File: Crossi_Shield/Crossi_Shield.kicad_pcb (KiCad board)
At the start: 4 copper layers, 86 parts, among them IC1 TPS54540DDAR, IC2 TCAN1048AVDMTRQ1, IC3 TCAN1048AVDMTRQ1, IC4 TCAN1048AVDMTRQ1, J1 Raspberry_Pi_2_3, J2 10090926-P444VLF, SW1 SW_DIP_x01

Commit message: Fast fertig gerouted
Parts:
- added H8: MountingHole, MountingHole:MountingHole_3.2mm_M3_DIN965_Pad, F.Cu at (141.5, 103.5)
- added H9: MountingHole, MountingHole:MountingHole_3.2mm_M3_DIN965_Pad, F.Cu at (141.5, 152.5)
- JP1, JP2, JP3, JP4, JP5: moved to B.Cu
- moved R6 69.6 mm to (144.6, 111.5), turned to 180 degrees
- moved D3 62.4 mm to (140.4, 111.5), turned to 0 degrees
- moved SW1 48.5 mm to (143.2, 115.5), turned to 180 degrees
- moved D5 34.4 mm to (83.0, 117.6), turned to 0 degrees
- moved R8 31.3 mm to (86.9, 117.6), turned to 180 degrees
- moved D6 30.1 mm to (83.0, 115.5), turned to 0 degrees
- moved R9 26.9 mm to (86.9, 115.5), turned to 180 degrees
- moved D7 26.1 mm to (83.0, 113.3), turned to 0 degrees
- moved R14 25.5 mm to (145.2, 139.2)
- moved R10 22.5 mm to (86.9, 113.3), turned to 180 degrees
- moved D8 22.1 mm to (83.0, 111.2), turned to 0 degrees
- moved R15 20.9 mm to (145.2, 141.2)
- moved IC2 19.1 mm to (136.7, 138.5)
- moved D4 18.5 mm to (83.0, 109.0), turned to 0 degrees
- moved R11 18.2 mm to (86.9, 111.2), turned to 180 degrees
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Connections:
- net Net-(IC1-SW) renamed /Versorgung/BOOT
- JP1 pad 2: Net-(H2-RXCAN) -> /CAN_Controller/CAN1_L
- JP2 pad 1: Net-(H1-RXCAN) -> /CAN_Controller/CAN0_L
- JP3 pad 1: Net-(H3-RXCAN) -> /CAN_Controller/CAN2_L
- JP4 pad 2: Net-(H4-RXCAN) -> /CAN_Controller/CAN3_L
- JP5 pad 1: Net-(H5-RXCAN) -> /CAN_Controller/CAN4_L
- R14 pad 1: Net-(H2-TXCAN) -> /CAN_Controller/CAN1_H
- R15 pad 2: Net-(H1-TXCAN) -> /CAN_Controller/CAN0_H
- R18 pad 2: Net-(H3-TXCAN) -> /CAN_Controller/CAN2_H
- R19 pad 1: Net-(H4-TXCAN) -> /CAN_Controller/CAN3_H
- R22 pad 2: Net-(H5-TXCAN) -> /CAN_Controller/CAN4_H
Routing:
- net Net-(H1-TXCAN): track 0.00 -> 70.7 mm, vias 0 -> 2
- net Net-(H1-RXCAN): track 0.00 -> 69.0 mm, vias 0 -> 2
- net Net-(H4-RXCAN): track 0.00 -> 63.2 mm, vias 0 -> 2
- net Net-(H2-TXCAN): track 0.00 -> 62.6 mm, vias 0 -> 2
- net Net-(H2-RXCAN): track 0.00 -> 61.1 mm, vias 0 -> 2
- net /CAN_Controller/INT4: track 0.00 -> 60.0 mm, vias 0 -> 2
- net Net-(J1-GPIO26): track 0.00 -> 58.3 mm, vias 0 -> 2
- net Net-(H4-TXCAN): track 0.00 -> 57.5 mm, vias 0 -> 2
- net /CAN_Controller/INT3: track 0.00 -> 54.1 mm, vias 0 -> 2
- net /CAN_Controller/INT0: track 0.00 -> 51.9 mm, vias 0 -> 2
- net /CAN_Controller/SCLK_1: track 0.00 -> 50.1 mm, vias 0 -> 4
- net /CAN_Controller/MOSI_1: track 0.00 -> 49.3 mm, vias 0 -> 4
- net /CAN_Controller/CE0_0: track 0.00 -> 48.9 mm, vias 0 -> 2
- net /CAN_Controller/INT2: track 0.00 -> 47.5 mm, vias 0 -> 4
- net /CAN_Controller/SCLK_0: track 0.00 -> 45.9 mm, vias 0 -> 5
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- added copper zone on F.Cu, net +5V
- added copper zone on In2.Cu, net +5V
- added copper zone on F.Cu, net /Versorgung/BOOT
- added copper zone on In1.Cu, net GND
- removed copper zone on In1.Cu, net +5V
- removed copper zone on In2.Cu, net GND

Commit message: arange device description
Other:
- board outline added: 84.9 x 55.8 mm

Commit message: some custom routs
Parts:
- moved JP2 6.92 mm to (146.2, 143.4)
- moved JP1 6.40 mm to (146.2, 139.2)
- moved JP4 4.93 mm to (146.2, 129.9)
- moved JP5 4.38 mm to (146.2, 125.2)
- moved JP3 1.14 mm to (146.2, 134.4)
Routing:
- net Net-(H1-TXCAN): track 70.7 -> 0.00 mm, vias 2 -> 0
- net Net-(H1-RXCAN): track 69.0 -> 0.00 mm, vias 2 -> 0
- net /Versorgung/VIN: track 65.6 -> 0.00 mm
- net Net-(H4-RXCAN): track 63.2 -> 0.00 mm, vias 2 -> 0
- net Net-(H2-TXCAN): track 62.6 -> 0.00 mm, vias 2 -> 0
- net Net-(H2-RXCAN): track 61.1 -> 0.00 mm, vias 2 -> 0
- net /CAN_Controller/INT4: track 60.0 -> 0.00 mm, vias 2 -> 0
- net Net-(J1-GPIO26): track 58.3 -> 0.00 mm, vias 2 -> 0
- net Net-(H4-TXCAN): track 57.5 -> 0.00 mm, vias 2 -> 0
- net /CAN_Controller/INT3: track 54.1 -> 0.00 mm, vias 2 -> 0
- net /CAN_Controller/INT0: track 51.9 -> 0.00 mm, vias 2 -> 0
- net /CAN_Controller/SCLK_1: track 50.1 -> 0.00 mm, vias 4 -> 0
- net /CAN_Controller/MOSI_1: track 49.1 -> 0.00 mm, vias 4 -> 0
- net /CAN_Controller/CE0_0: track 48.9 -> 0.00 mm, vias 2 -> 0
- net /CAN_Controller/INT2: track 47.5 -> 0.00 mm, vias 4 -> 0
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
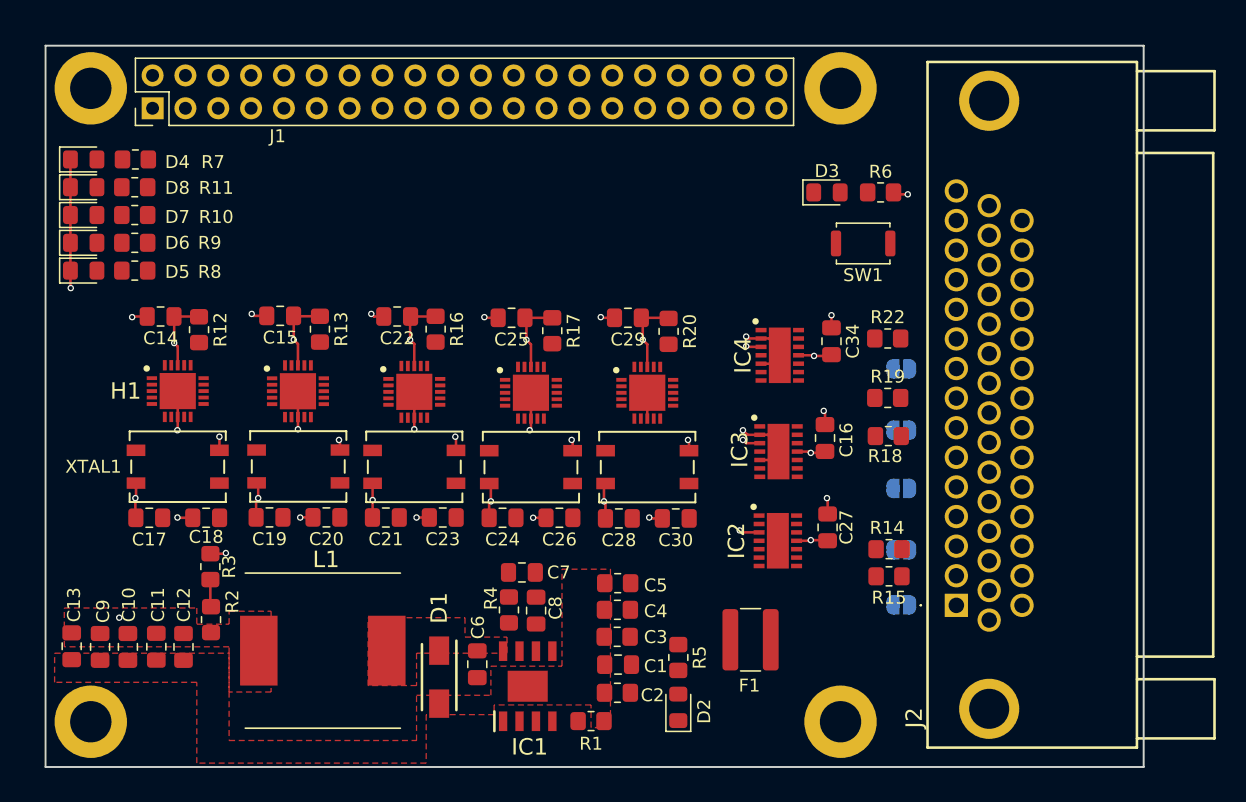
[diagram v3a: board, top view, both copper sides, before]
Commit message: new buckconf design
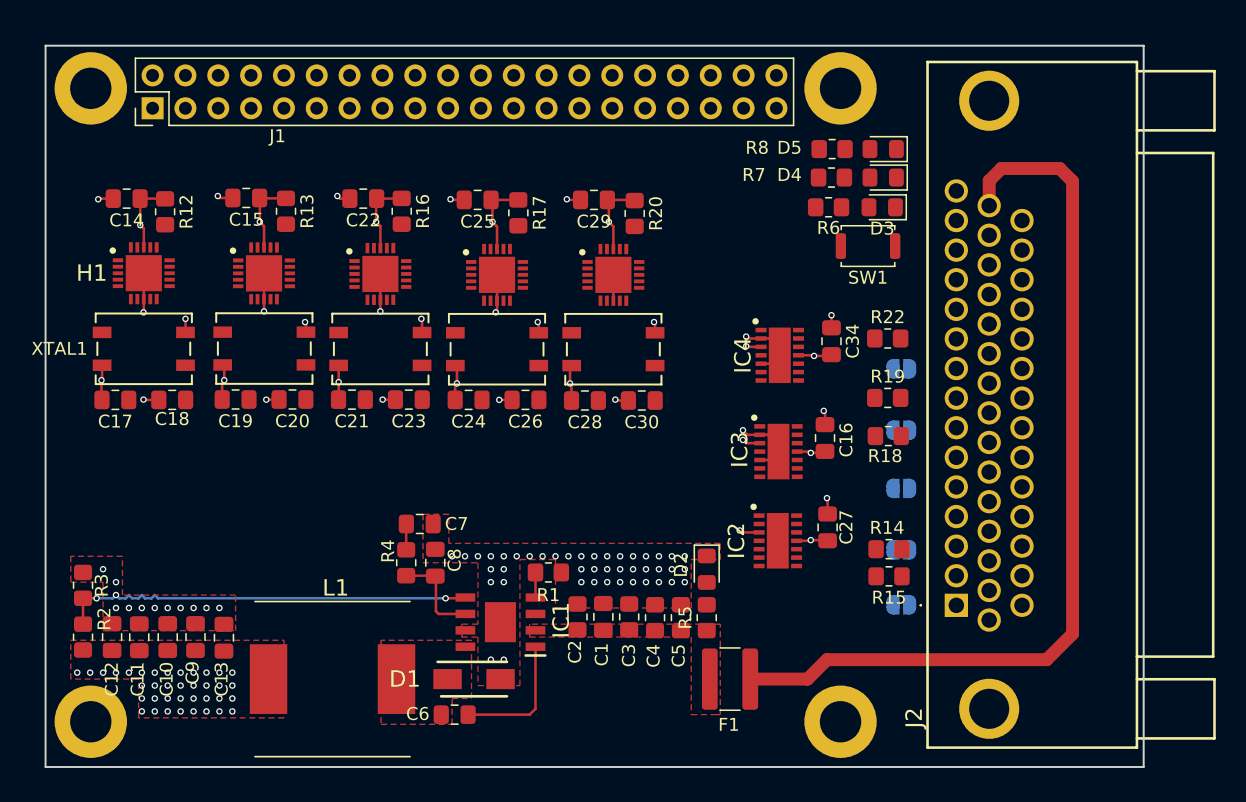
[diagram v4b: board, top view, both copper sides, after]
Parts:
- removed D6, D7, D8: LED, LED_SMD:LED_0805_2012Metric_Pad1.15x1.40mm_HandSolder
- removed R10, R11, R9: 510R, Resistor_SMD:R_0805_2012Metric_Pad1.20x1.40mm_HandSolder
- moved D5 62.6 mm to (144.8, 108.2), turned to 180 degrees
- moved D4 61.9 mm to (144.8, 110.4), turned to 180 degrees
- moved R8 54.8 mm to (140.8, 108.2), turned to 0 degrees
- moved R7 53.9 mm to (140.8, 110.4), turned to 0 degrees
- moved R1 12.0 mm to (118.9, 140.9)
- moved C13 11.8 mm to (93.8, 146.0), turned to 90 degrees
- moved D2 10.9 mm to (131.2, 140.7), turned to -90 degrees
- moved R2 9.99 mm to (82.9, 145.9)
- moved R3 9.96 mm to (82.9, 141.9)
- moved C14 9.49 mm to (86.3, 112.0)
- moved C18 9.49 mm to (89.8, 127.6)
- moved C19 9.49 mm to (94.7, 127.6)
- moved C20 9.49 mm to (99.1, 127.6)
- moved C22 9.49 mm to (104.6, 112.0)
- moved C24 9.49 mm to (112.7, 127.6)
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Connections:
- J1 pad 16: Net-(J1-GPIO23) -> unconnected-(J1-GPIO23-Pad16)
- J1 pad 18: Net-(J1-GPIO24) -> unconnected-(J1-GPIO24-Pad18)
- J1 pad 22: Net-(J1-GPIO25) -> unconnected-(J1-GPIO25-Pad22)
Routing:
- net /Versorgung/VIN: track 0.00 -> 70.6 mm
- net Net-(IC1-FB): track 2.12 -> 32.4 mm, vias 0 -> 3
- net GND: track 68.7 -> 57.5 mm, vias 31 -> 83
- net Net-(IC1-BOOT): track 0.00 -> 10.2 mm
- net Net-(IC1-COMP): track 0.00 -> 7.36 mm
- net Net-(C7-Pad1): track 0.00 -> 2.01 mm
- net Net-(IC1-RT/CLK): track 0.00 -> 1.94 mm
- net +5V: track 43.1 -> 42.2 mm, vias 13 -> 48
- added copper zone on F.Cu, net /Versorgung/VIN_SAVE

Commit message: fix netlist bug and filled g&b with copper
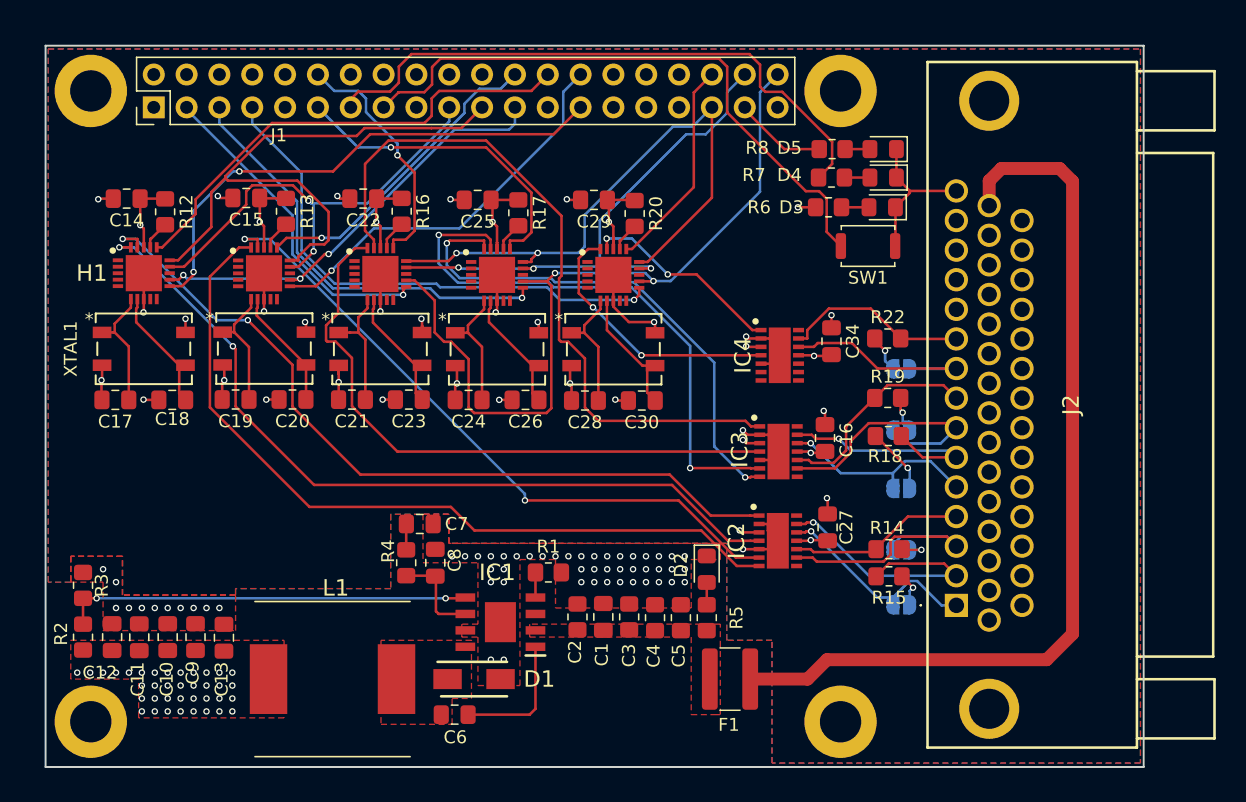
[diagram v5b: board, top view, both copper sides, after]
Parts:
- moved J1 24.3 mm to (112.5, 103.7)
- moved H6 0.20 mm to (83.5, 103.7)
- moved H8 0.20 mm to (141.5, 103.7)
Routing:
- net Net-(H1-RXCAN): track 0.00 -> 62.4 mm, vias 0 -> 2
- net Net-(H2-RXCAN): track 0.00 -> 61.8 mm
- net Net-(H1-TXCAN): track 0.00 -> 61.8 mm, vias 0 -> 2
- net /CAN_Controller/SCLK_1: track 0.00 -> 61.7 mm, vias 0 -> 2
- net Net-(H3-TXCAN): track 0.00 -> 55.3 mm
- net Net-(H2-TXCAN): track 0.00 -> 51.9 mm, vias 0 -> 2
- net Net-(H3-RXCAN): track 0.00 -> 48.3 mm
- net Net-(J1-GPIO22): track 0.00 -> 47.3 mm
- net Net-(J1-GPIO27): track 0.00 -> 47.1 mm
- net /CAN_Controller/MISO_1: track 0.00 -> 46.2 mm, vias 0 -> 2
- net /CAN_Controller/MISO_0: track 0.00 -> 45.8 mm
- net Net-(H4-TXCAN): track 0.00 -> 44.0 mm, vias 0 -> 2
- net /CAN_Controller/MOSI_1: track 0.00 -> 41.2 mm, vias 0 -> 3
- net /CAN_Controller/INT4: track 0.00 -> 41.1 mm, vias 0 -> 1
- net /CAN_Controller/INT0: track 0.00 -> 40.4 mm, vias 0 -> 2
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- added copper zone on B.Cu, net GND
